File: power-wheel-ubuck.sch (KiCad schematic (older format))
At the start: 23 parts, among them J1 CONN_01X02_MALE, J10 TEST_1P, J2 TEST_1P, J3 TEST_1P, J4 CONN_01X03_MALE, J5 TEST_1P, J6 TEST_1P, J7 TEST_1P, J8 TEST_1P, J9 CONN_01X02_MALE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

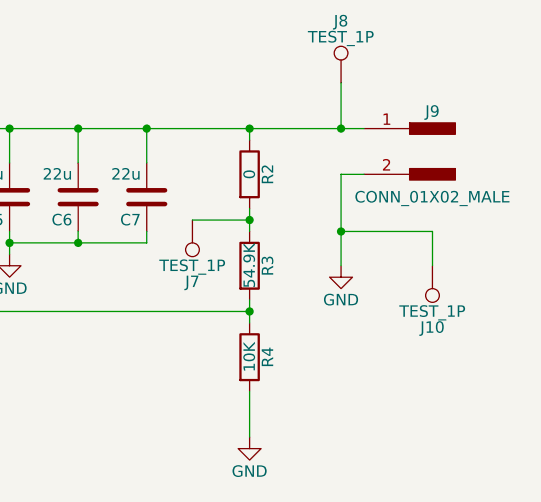
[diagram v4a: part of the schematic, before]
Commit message: Remove redundant testpoint
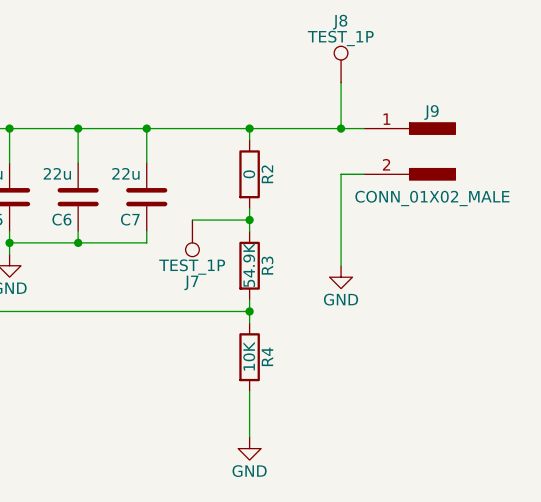
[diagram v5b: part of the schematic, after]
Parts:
- removed J10: TEST_1P, Measurement_Points:Measurement_Point_Square-SMD-Pad_Big, symbol TEST_1P
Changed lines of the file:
@@
 Wire Wire Line
 	8800 3700 8800 4100
-$Comp
-L TEST_1P J10
-U 1 1 594643F3
-P 9200 4100
-F 0 "J10" H 9200 4370 50  0000 C CNN
-F 1 "TEST_1P" H 9200 4300 50  0000 C CNN
-F 2 "Measurement_Points:Measurement_Point_Square-SMD-Pad_Big" H 9400 4100 50  0001 C CNN
-F 3 "" H 9400 4100 50  0001 C CNN
-	1    9200 4100
-	-1   0    0    1
-$EndComp
-Wire Wire Line
-	9200 4100 9200 3950
-Wire Wire Line
-	9200 3950 8800 3950
-Connection ~ 8800 3950
 $EndSCHEMATC

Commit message: Smaller test pad points
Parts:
- J2, J3, J5, J6, J7, J8: footprint Measurement_Points:Measurement_Point_Square-SMD-Pad_Big -> Measurement_Points:Measurement_Point_Square-SMD-Pad_Small
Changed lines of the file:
@@
 F 0 "J2" H 2400 3370 50  0000 C CNN
 F 1 "TEST_1P" H 2400 3300 50  0000 C CNN
-F 2 "Measurement_Points:Measurement_Point_Square-SMD-Pad_Big" H 2600 3100 50  0001 C CNN
+F 2 "Measurement_Points:Measurement_Point_Square-SMD-Pad_Small" H 2600 3100 50  0001 C CNN
 F 3 "" H 2600 3100 50  0001 C CNN
 	1    2400 3100
@@
 F 0 "J3" H 2500 4370 50  0000 C CNN
 F 1 "TEST_1P" H 2500 4300 50  0000 C CNN
-F 2 "Measurement_Points:Measurement_Point_Square-SMD-Pad_Big" H 2700 4100 50  0001 C CNN
+F 2 "Measurement_Points:Measurement_Point_Square-SMD-Pad_Small" H 2700 4100 50  0001 C CNN
 F 3 "" H 2700 4100 50  0001 C CNN
 	1    2500 4100
@@
 F 0 "J5" H 4400 4420 50  0000 C CNN
 F 1 "TEST_1P" H 4400 4350 50  0000 C CNN
-F 2 "Measurement_Points:Measurement_Point_Square-SMD-Pad_Big" H 4600 4150 50  0001 C CNN
+F 2 "Measurement_Points:Measurement_Point_Square-SMD-Pad_Small" H 4600 4150 50  0001 C CNN
 F 3 "" H 4600 4150 50  0001 C CNN
 	1    4400 4150
@@
 F 0 "J6" H 6600 3870 50  0000 C CNN
 F 1 "TEST_1P" H 6600 3800 50  0000 C CNN
-F 2 "Measurement_Points:Measurement_Point_Square-SMD-Pad_Big" H 6800 3600 50  0001 C CNN
+F 2 "Measurement_Points:Measurement_Point_Square-SMD-Pad_Small" H 6800 3600 50  0001 C CNN
 F 3 "" H 6800 3600 50  0001 C CNN
 	1    6600 3600
@@
 F 0 "J7" H 8150 4170 50  0000 C CNN
 F 1 "TEST_1P" H 8150 4100 50  0000 C CNN
-F 2 "Measurement_Points:Measurement_Point_Square-SMD-Pad_Big" H 8350 3900 50  0001 C CNN
+F 2 "Measurement_Points:Measurement_Point_Square-SMD-Pad_Small" H 8350 3900 50  0001 C CNN
 F 3 "" H 8350 3900 50  0001 C CNN
 	1    8150 3900
@@
 F 0 "J8" H 8800 3570 50  0000 C CNN
 F 1 "TEST_1P" H 8800 3500 50  0000 C CNN
-F 2 "Measurement_Points:Measurement_Point_Square-SMD-Pad_Big" H 9000 3300 50  0001 C CNN
+F 2 "Measurement_Points:Measurement_Point_Square-SMD-Pad_Small" H 9000 3300 50  0001 C CNN
 F 3 "" H 9000 3300 50  0001 C CNN
 	1    8800 3300

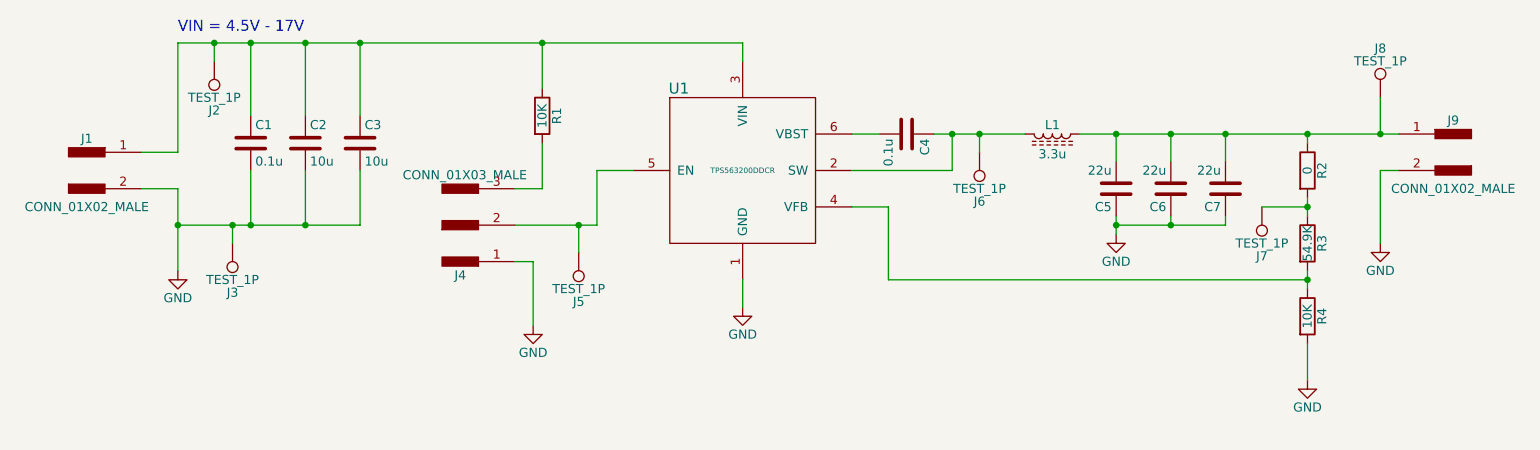
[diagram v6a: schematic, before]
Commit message: Removed the "jumper switch" and moved things in to fill the hole
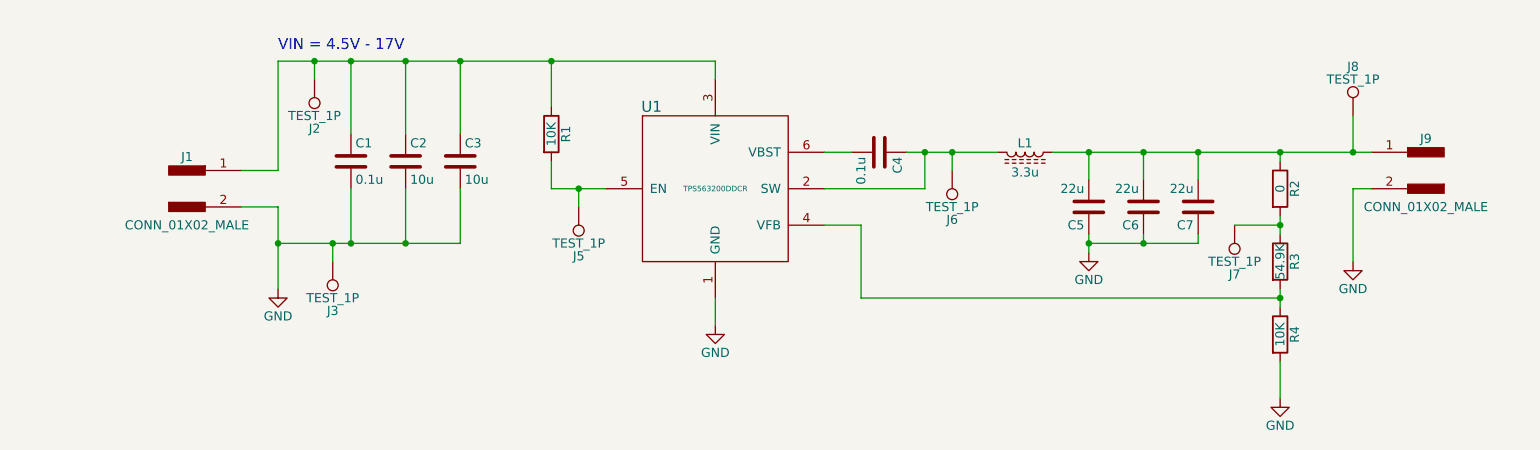
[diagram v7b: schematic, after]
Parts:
- removed J4: CONN_01X03_MALE, Pin_Headers:Pin_Header_Straight_1x03_Pitch2.54mm, symbol CONN_01X03_MALE
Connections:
- net at J5.1, U1.5 (EN): now also R1.2
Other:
- moved on the sheet: C1, C2, C3, C4, C5, C6, C7, J1, J2, J3, J5, J6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

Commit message: Add part numbers and links to the capacitors
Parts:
- C1, C4: DKPN (none) -> 311-1140-1-ND; MPN (none) -> CC0805KRX7R9BB104
- C2, C3: DKPN (none) -> 490-5523-1-ND; MPN (none) -> GRM21BR61E106KA73L
- C5, C6, C7: DKPN (none) -> 1276-6780-1-ND; MPN (none) -> CL21A226MOCLRNC
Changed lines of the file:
@@
 F 1 "0.1u" H 3175 3550 50  0000 L CNN
 F 2 "Capacitors_SMD:C_0805_HandSoldering" H 3188 3500 50  0001 C CNN
-F 3 "" H 3150 3650 50  0001 C CNN
+F 3 "http://www.yageo.com/documents/recent/UPY-GPHC_X7R_6.3V-to-50V_18.pdf" H 3150 3650 50  0001 C CNN
+F 4 "CC0805KRX7R9BB104" H 3150 3650 60  0001 C CNN "MPN"
+F 5 "311-1140-1-ND" H 3150 3650 60  0001 C CNN "DKPN"
 	1    3150 3650
 	1    0    0    -1
@@
 F 1 "10u" H 3475 3550 50  0000 L CNN
 F 2 "Capacitors_SMD:C_0805_HandSoldering" H 3488 3500 50  0001 C CNN
-F 3 "" H 3450 3650 50  0001 C CNN
+F 3 "http://search.murata.co.jp/Ceramy/image/img/A01X/G101/ENG/GRM21BR61E106KA73-01.pdf" H 3450 3650 50  0001 C CNN
+F 4 "GRM21BR61E106KA73L" H 3450 3650 60  0001 C CNN "MPN"
+F 5 "490-5523-1-ND" H 3450 3650 60  0001 C CNN "DKPN"
 	1    3450 3650
 	1    0    0    -1
@@
 F 1 "10u" H 3775 3550 50  0000 L CNN
 F 2 "Capacitors_SMD:C_0805_HandSoldering" H 3788 3500 50  0001 C CNN
-F 3 "" H 3750 3650 50  0001 C CNN
+F 3 "http://search.murata.co.jp/Ceramy/image/img/A01X/G101/ENG/GRM21BR61E106KA73-01.pdf" H 3750 3650 50  0001 C CNN
+F 4 "GRM21BR61E106KA73L" H 3750 3650 60  0001 C CNN "MPN"
+F 5 "490-5523-1-ND" H 3750 3650 60  0001 C CNN "DKPN"
 	1    3750 3650
 	1    0    0    -1
@@
 F 1 "0.1u" H 6075 3500 50  0000 L CNN
 F 2 "Capacitors_SMD:C_0805_HandSoldering" H 6088 3450 50  0001 C CNN
-F 3 "" H 6050 3600 50  0001 C CNN
+F 3 "http://www.yageo.com/documents/recent/UPY-GPHC_X7R_6.3V-to-50V_18.pdf" H 6050 3600 50  0001 C CNN
+F 4 "CC0805KRX7R9BB104" H 6050 3600 60  0001 C CNN "MPN"
+F 5 "311-1140-1-ND" H 6050 3600 60  0001 C CNN "DKPN"
 	1    6050 3600
 	0    1    1    0
@@
 F 1 "22u" H 7225 3800 50  0000 L CNN
 F 2 "Capacitors_SMD:C_0805_HandSoldering" H 7238 3750 50  0001 C CNN
-F 3 "" H 7200 3900 50  0001 C CNN
+F 3 "http://www.samsungsem.com/kr/support/library/product-catalog/mlcc.jsp" H 7200 3900 50  0001 C CNN
+F 4 "CL21A226MOCLRNC" H 7200 3900 60  0001 C CNN "MPN"
+F 5 "1276-6780-1-ND" H 7200 3900 60  0001 C CNN "DKPN"
 	1    7200 3900
 	-1   0    0    1
@@
 F 1 "22u" H 7525 3800 50  0000 L CNN
 F 2 "Capacitors_SMD:C_0805_HandSoldering" H 7538 3750 50  0001 C CNN
-F 3 "" H 7500 3900 50  0001 C CNN
+F 3 "http://www.samsungsem.com/kr/support/library/product-catalog/mlcc.jsp" H 7500 3900 50  0001 C CNN
+F 4 "CL21A226MOCLRNC" H 7500 3900 60  0001 C CNN "MPN"
+F 5 "1276-6780-1-ND" H 7500 3900 60  0001 C CNN "DKPN"
 	1    7500 3900
 	-1   0    0    1
@@
 F 1 "22u" H 7825 3800 50  0000 L CNN
 F 2 "Capacitors_SMD:C_0805_HandSoldering" H 7838 3750 50  0001 C CNN
-F 3 "" H 7800 3900 50  0001 C CNN
+F 3 "http://www.samsungsem.com/kr/support/library/product-catalog/mlcc.jsp" H 7800 3900 50  0001 C CNN
+F 4 "CL21A226MOCLRNC" H 7800 3900 60  0001 C CNN "MPN"
+F 5 "1276-6780-1-ND" H 7800 3900 60  0001 C CNN "DKPN"
 	1    7800 3900
 	-1   0    0    1
